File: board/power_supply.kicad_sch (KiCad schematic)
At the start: 54 parts, among them J1 USB, J2 LiPo, U1 IP5306, U2 TPS562201, U3 RT9069, U4 TPS55340PWP

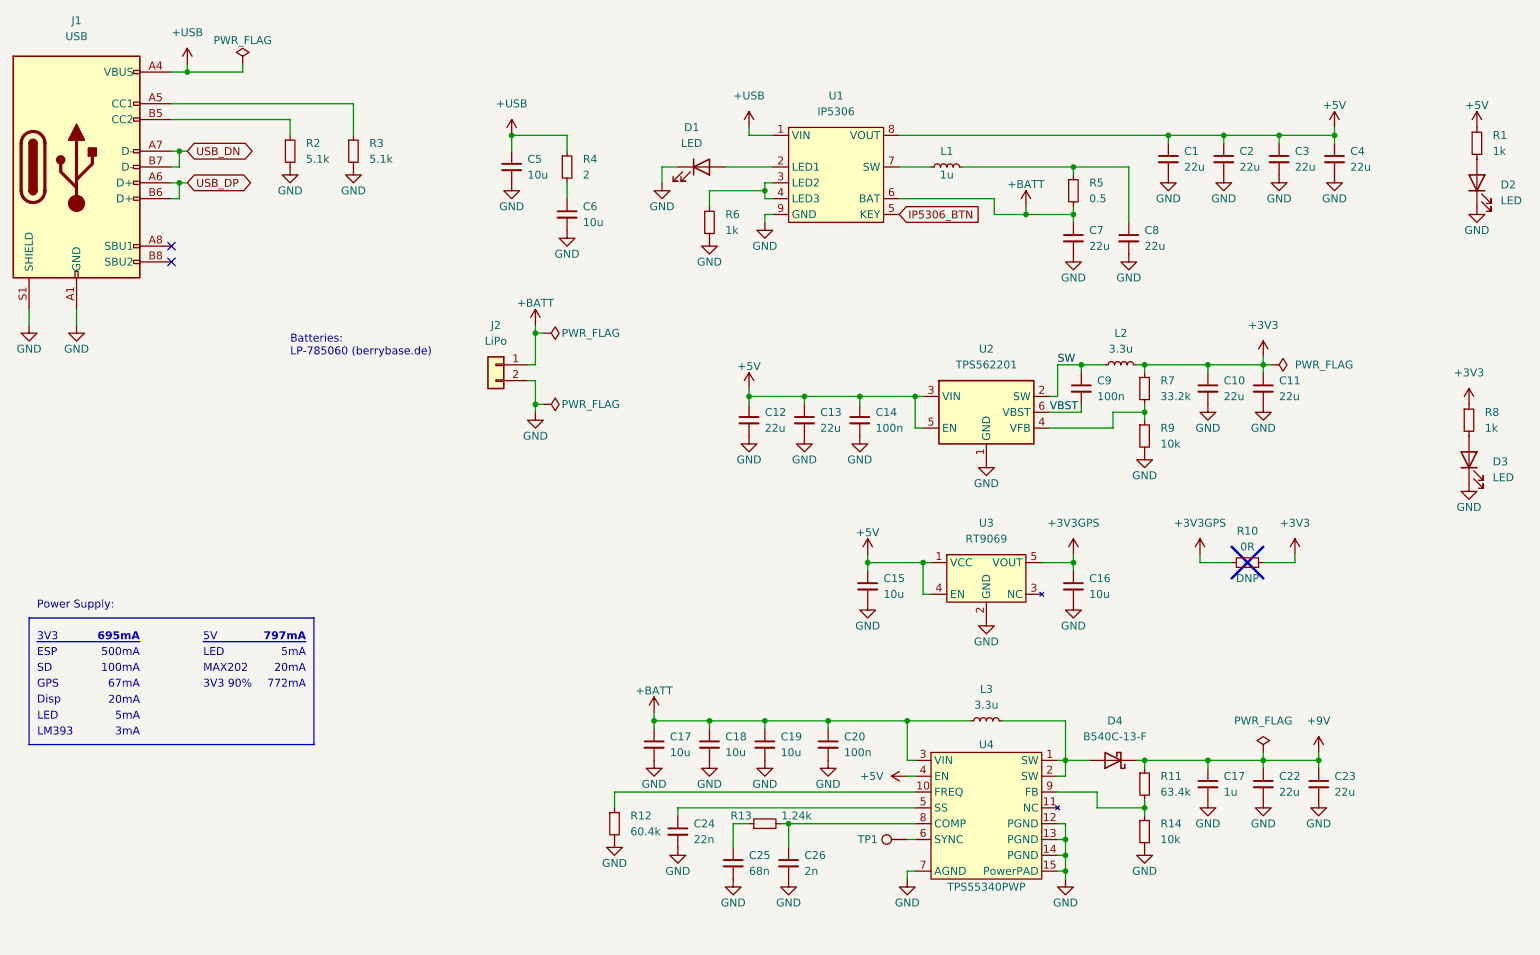
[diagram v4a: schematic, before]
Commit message: Rough placement of US electronics
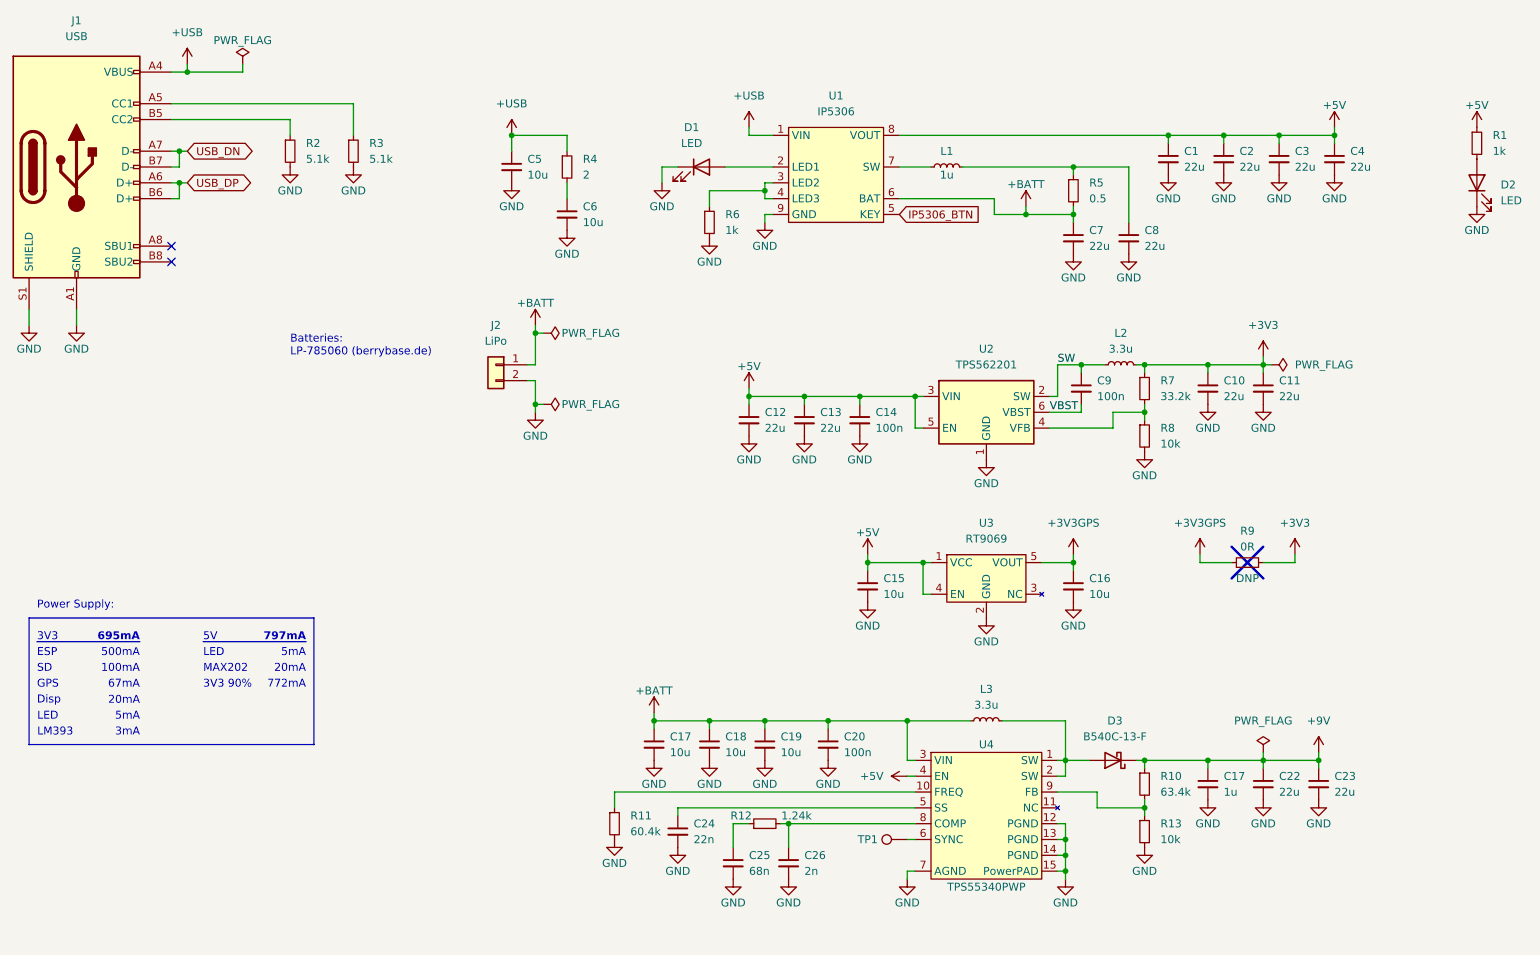
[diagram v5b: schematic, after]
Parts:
- removed D3: LED, LED_SMD:LED_0603_1608Metric, symbol Device:LED
- removed R8: 1k, Resistor_SMD:R_0603_1608Metric, symbol Device:R_Small
- renumbered D4 to D3, R11 to R10, R12 to R11, R13 to R12, R14 to R13, R9 to R8, R10 to R9

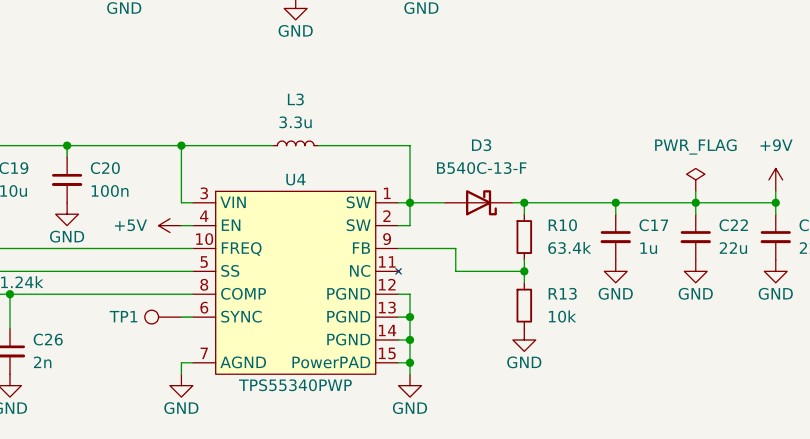
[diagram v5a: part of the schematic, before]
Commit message: 3D-Modelle hinzugefügt
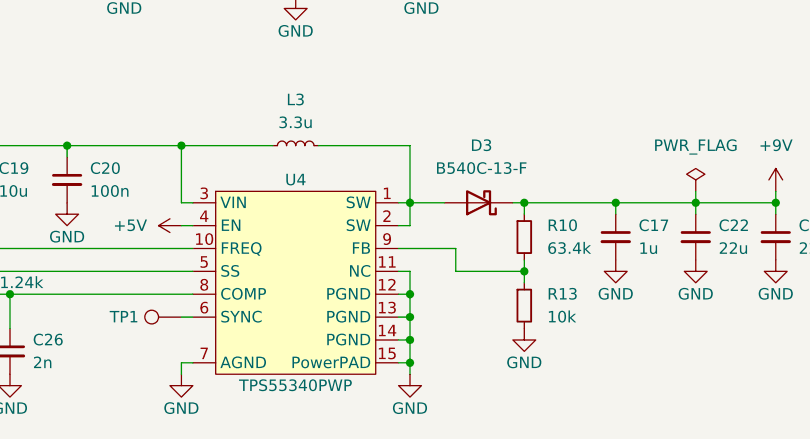
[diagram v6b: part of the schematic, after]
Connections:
- net GND: now also U4.11 (NC)
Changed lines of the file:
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@@
   (junction (at 151.13 147.32) (diameter 0) (color 0 0 0 0)
+  )
+  (junction (at 195.58 147.32) (diameter 0) (color 0 0 0 0)
   )
   (junction (at 106.68 36.83) (diameter 0) (color 0 0 0 0)
@@
   (no_connect (at 52.07 54.61))
   (no_connect (at 52.07 57.15))
-  (wire (pts (xy 194.31 147.32) (xy 195.58 147.32))
-    (stroke (width 0) (type default))
-  )
   (wire (pts (xy 170.18 139.7) (xy 171.45 139.7))
     (stroke (width 0) (type default))
@@
   )
   (wire (pts (xy 207.01 73.66) (xy 208.28 73.66))
+    (stroke (width 0) (type default))
+  )
+  (wire (pts (xy 195.58 144.78) (xy 195.58 147.32))
     (stroke (width 0) (type default))
   )
@@
     (stroke (width 0) (type default))
   )
+  (wire (pts (xy 195.58 147.32) (xy 194.31 147.32))
+    (stroke (width 0) (type default))
+  )
   (wire (pts (xy 220.98 36.83) (xy 220.98 38.1))
     (stroke (width 0) (type default))
@@
     (stroke (width 0) (type default))
   )
+  (wire (pts (xy 194.31 144.78) (xy 195.58 144.78))
+    (stroke (width 0) (type default))
+  )

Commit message: Routing basically finished
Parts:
- removed U4: TPS55340PWP, OBSPro:TSSOP-14-1EP_2.6x2.6mm_P0.65mm, symbol OBSPro:TPS55340PWP
- added U4: ~, Package_DFN_QFN:VQFN-16-1EP_3x3mm_P0.5mm_EP1.68x1.68mm, symbol OBSPro:TPS55340R
- J2: MF JST -> (none); Manufacturer (none) -> JST
- R1: value 1k -> 10k; JLC_PN C21190 -> C25804; JLC_Price10 0.0005 -> 0.0013; MPN 0603WAF1001T5E -> 0603WAF1002T5E; PCBA yes -> (none); kicost:JLC:pricing 1: USD 0.0005; 200: USD 0.0004 -> (none)
- R13, R8: JLC_PN C25197 -> C25804; MPN 0603WAF510KT5E -> 0603WAF1002T5E
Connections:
- net +5V: now also U4.3 (EN)
- net +BATT: now also R6.2, U4.2 (VIN)
- net GND: now also U4.10 (NC), U4.11 (PGND), U4.12 (PGND), U4.13 (PGND), U4.14 (NC), U4.17 (PowerPAD), U4.6 (AGND); no longer R6.2
- net at C26.1, R12.2: now also U4.7 (COMP)
- net at D3.2 (A), L3.2: now also U4.1 (SW), U4.15 (SW), U4.16 (SW)
- net at R10.2, R13.1: now also U4.8 (FB)
- net at R11.1: now also U4.9 (FREQ)
- net at TP1.1: now also U4.5 (SYNC)
- net at C24.1: now also U4.4 (SS)

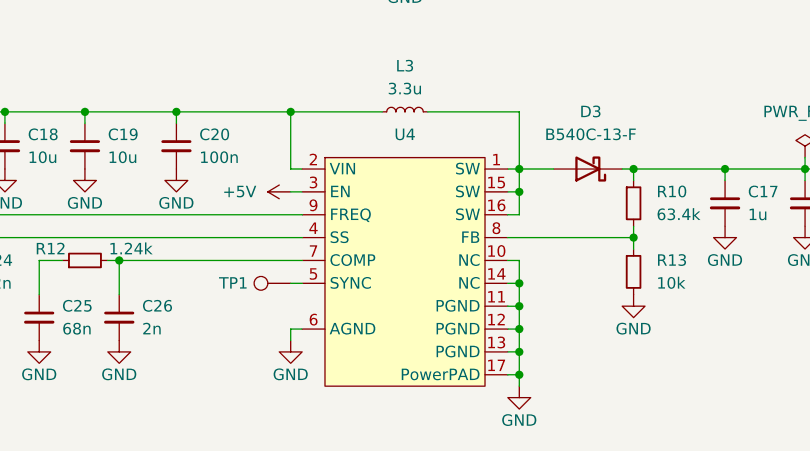
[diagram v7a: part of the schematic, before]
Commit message: Added beads, fixed a few part numbers, exported gerber/drill This is the ordered version
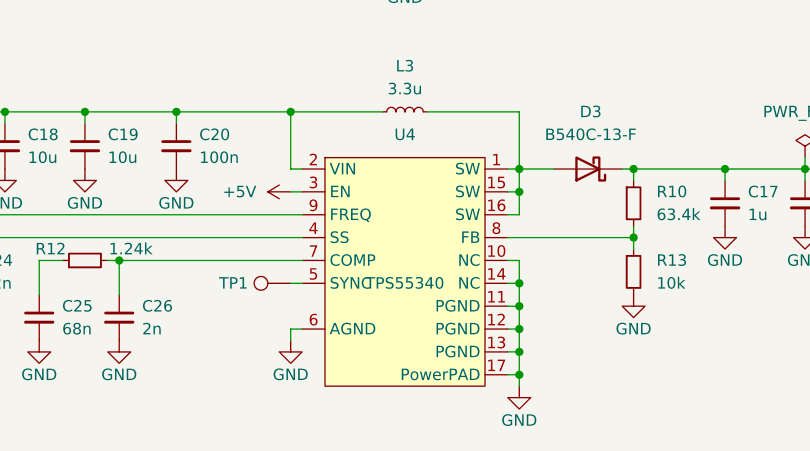
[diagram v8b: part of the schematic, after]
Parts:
- U4: value ~ -> TPS55340; JLC_PN (none) -> C169167
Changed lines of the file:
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@@
       (effects (font (size 1.27 1.27)))
     )
-    (property "Value" "~" (at 182.88 149.86 0)
+    (property "Value" "TPS55340" (at 182.88 149.86 0)
       (effects (font (size 1.27 1.27)))
     )
@@
       (effects (font (size 1.27 1.27)) hide)
     )
+    (property "JLC_PN" "C169167" (at 182.88 147.32 0)
+      (effects (font (size 1.27 1.27)) hide)
+    )
